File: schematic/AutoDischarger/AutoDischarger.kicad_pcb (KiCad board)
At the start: 4 copper layers, 50 x 50 mm, 79 parts, among them IC1 AP7375-50W5-7, IC2 PIC18F15Q40-I_SS, IC3 TLV9102SIDGSR, IC4 TLV9102SIDGSR, IC5 TLV9102SIDGSR, J1 ICSP, J2 Balance Lead, Q1 2N7002_HAMR, Q10 2N7002_HAMR, Q11 2N7002_HAMR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

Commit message: Generated gerbers
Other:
- outline, holes or cut-outs redrawn
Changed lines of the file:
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@@
   (gr_poly
     (pts
-      (xy 109.4 88.8)
-      (xy 107.7 90.3)
-      (xy 107.7 87.3)
+      (xy 109.6 88.8)
+      (xy 107.9 90.3)
+      (xy 107.9 87.3)
     ) (layer "F.SilkS") (width 0.16) (fill solid))
   (gr_line (start 131.5 94.1) (end 132.5 94.9) (layer "F.SilkS") (width 0.2))
-  (gr_rect locked (start 107 86) (end 157 136) (layer "Edge.Cuts") (width 0.1) (fill none))
+  (gr_line (start 154.2 86) (end 109.779899 85.979899) (layer "Edge.Cuts") (width 0.05))
+  (gr_line (start 106.979899 88.779899) (end 107 133.2) (layer "Edge.Cuts") (width 0.05))
+  (gr_arc (start 154.2 86) (mid 156.179899 86.820101) (end 157 88.8) (layer "Edge.Cuts") (width 0.05))
+  (gr_arc (start 106.979899 88.779899) (mid 107.8 86.8) (end 109.779899 85.979899) (layer "Edge.Cuts") (width 0.05))
+  (gr_line (start 157 133.2) (end 157 88.8) (layer "Edge.Cuts") (width 0.05))
+  (gr_line (start 109.8 136) (end 154.2 136) (layer "Edge.Cuts") (width 0.05))
+  (gr_arc (start 157 133.2) (mid 156.179899 135.179899) (end 154.2 136) (layer "Edge.Cuts") (width 0.05))
+  (gr_arc (start 109.8 136) (mid 107.820101 135.179899) (end 107 133.2) (layer "Edge.Cuts") (width 0.05))
   (gr_text "JP1=3S\nJP2=4S   23=enable\nJP3=5S   12=disable \nJP4=6S" (at 127.2 117) (layer "B.SilkS")
     (effects (font (size 1 1) (thickness 0.16)) (justify left mirror))

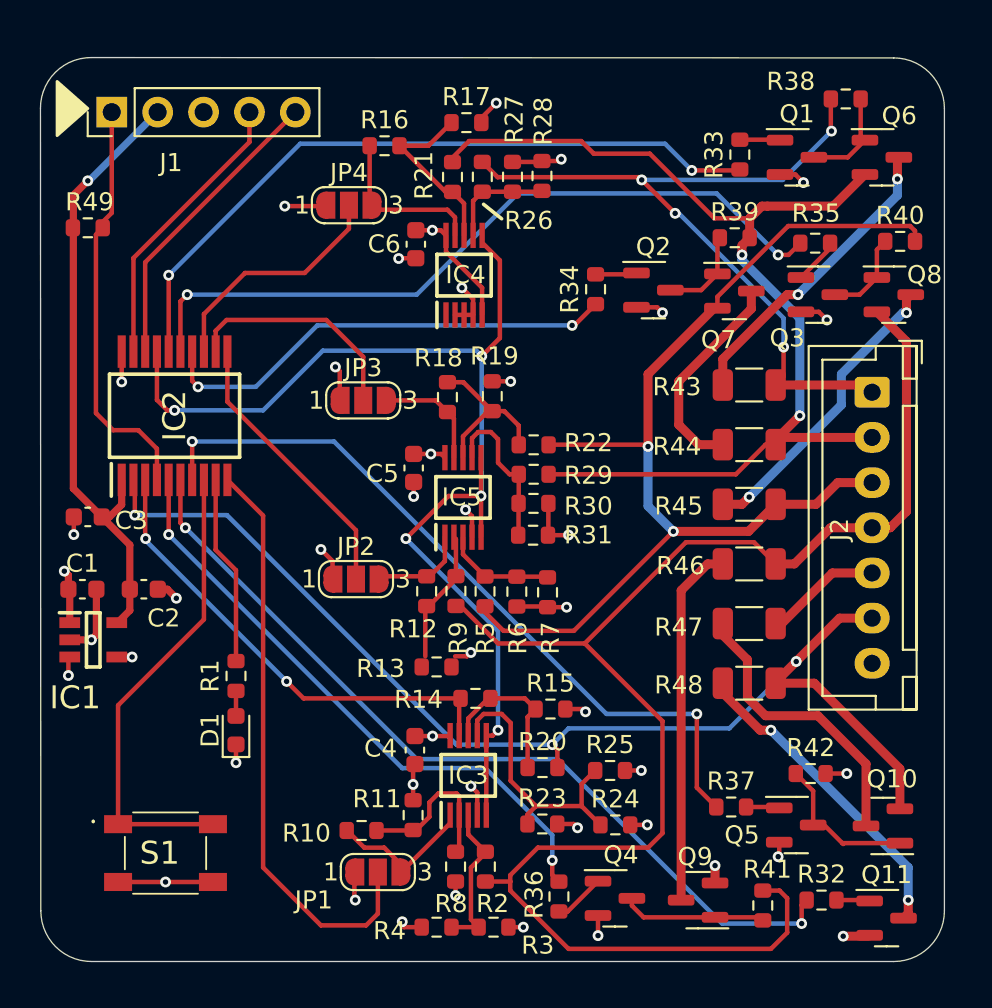
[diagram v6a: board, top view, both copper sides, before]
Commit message: Updated for 18R 1W 2512 resistors
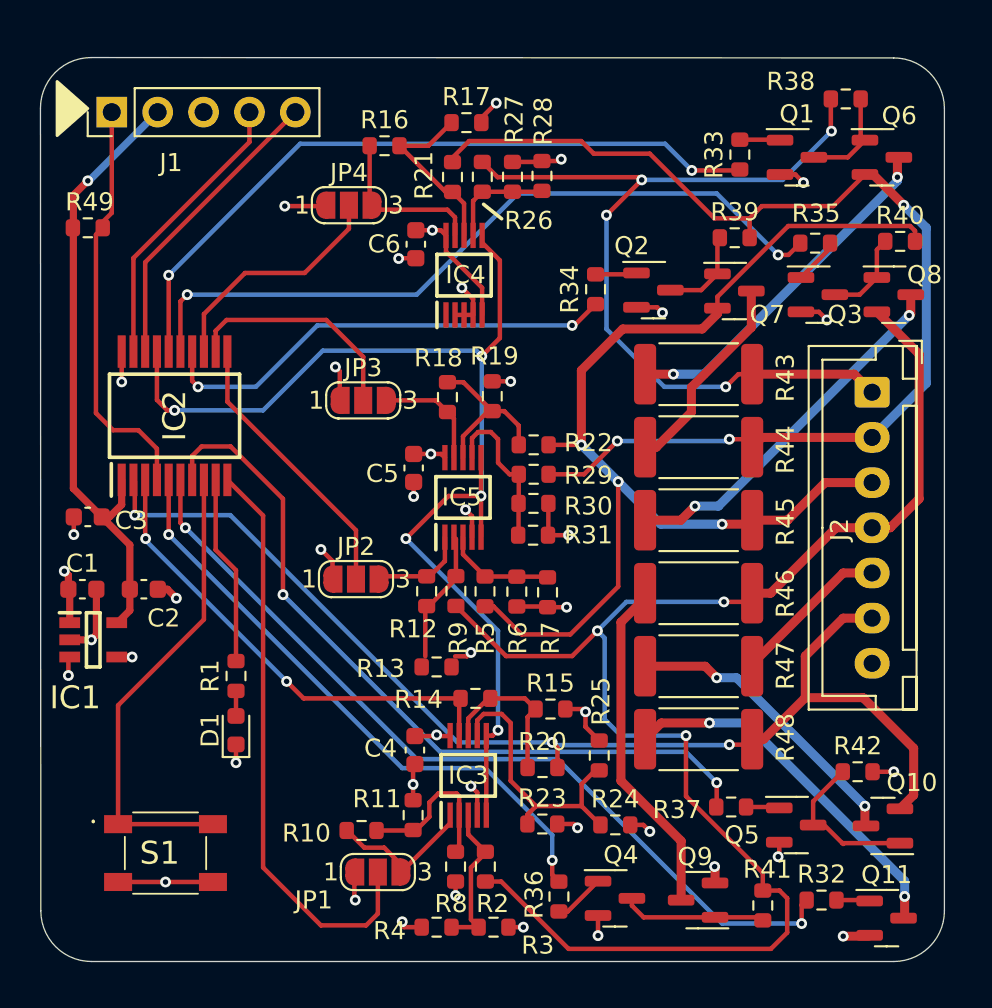
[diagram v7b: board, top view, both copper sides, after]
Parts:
- R43, R44, R45, R46, R47, R48: value 120R -> 18R; footprint Resistor_SMD:R_1206_3216Metric -> Resistor_SMD:R_2512_6332Metric
- moved R48 4.18 mm to (143.4, 123.7)
- moved R47 3.66 mm to (143.4, 119.7)
- moved R46 3.23 mm to (143.4, 115.6)
- moved R45 2.94 mm to (143.4, 111.6)
- moved R43 2.86 mm to (143.4, 103.5)
- moved R44 2.80 mm to (143.4, 107.5)
- moved R42 2.60 mm to (152.2, 125.5)
- moved R25 1.02 mm to (137.9, 124.6), turned to 90 degrees
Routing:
- net /Discharge Control/VC6: track 41.9 -> 48.4 mm
- net Net-(Q8-Pad3): track 16.6 -> 20.5 mm
- net /Discharge Control/VC5: track 59.1 -> 62.6 mm, vias 2 -> 3
- net Net-(Q11-Pad3): track 17.2 -> 20.4 mm
- net /Discharge Control/VC4: track 59.4 -> 62.4 mm, vias 2 -> 3
- net Net-(Q6-Pad3): track 16.9 -> 19.7 mm
- net /Discharge Control/VC3: track 85.6 -> 83.3 mm, vias 0 -> 3
- net +8V: track 25.4 -> 27.4 mm
- net Net-(Q9-Pad3): track 20.1 -> 18.6 mm
- net GND: track 57.2 -> 58.5 mm, vias 34 -> 33
- net /Discharge Control/C2: track 41.9 -> 42.7 mm
- net /Discharge Control/VC1: track 64.9 -> 64.1 mm
- net Net-(Q7-Pad3): track 12.0 -> 11.4 mm
- net Net-(Q10-Pad3): track 16.2 -> 16.5 mm, vias 0 -> 2
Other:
- board text added: "AutoDischarger V1.1 QES 2023"
- board text removed: "AutoDischarger V1.0 QES 2022"

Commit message: Some improvements and new gerbers
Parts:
- moved JP1 0.65 mm to (125.6, 131.7)
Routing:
- net /Voltage Sense/V_SENSE3: track 32.5 -> 26.3 mm
- net /Voltage Sense/SHDN: track 64.7 -> 60.2 mm, vias 5 -> 4
- net Net-(IC3-Pad1): track 7.61 -> 10.9 mm
- net /Discharge Control/VC3: track 83.3 -> 80.9 mm
- net /Discharge Control/VC5: track 62.6 -> 61.6 mm
- net Net-(Q8-Pad3): track 20.5 -> 21.3 mm
